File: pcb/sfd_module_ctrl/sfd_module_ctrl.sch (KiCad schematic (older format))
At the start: 12 parts

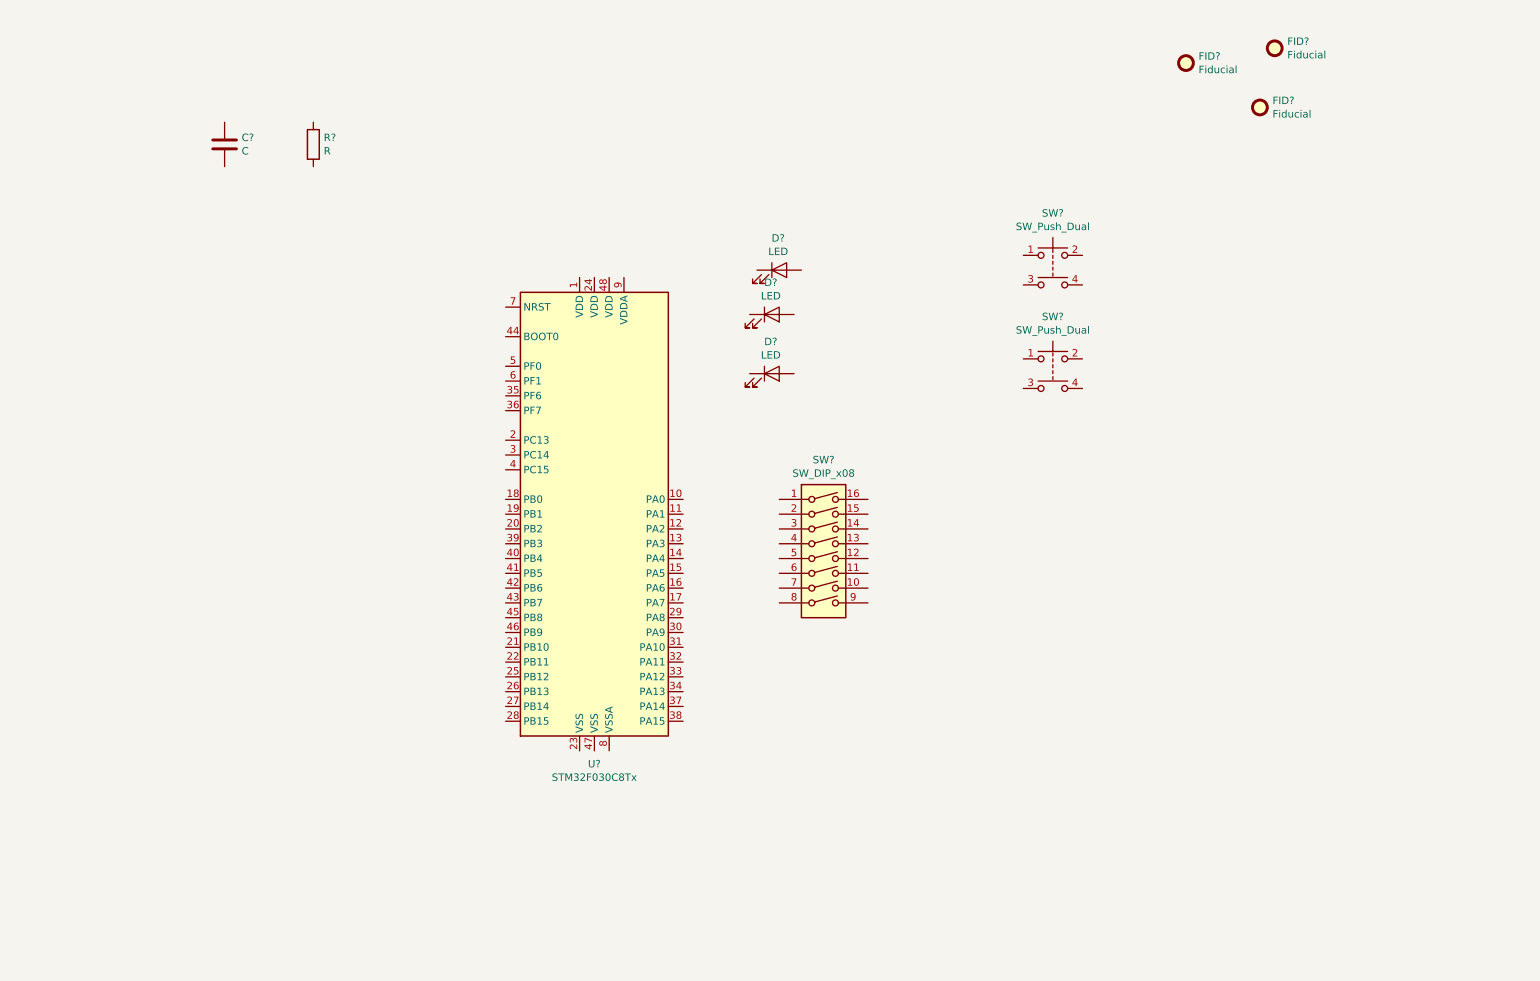
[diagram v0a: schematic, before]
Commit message: schematic progress, added stm32cubeMX generated chip config
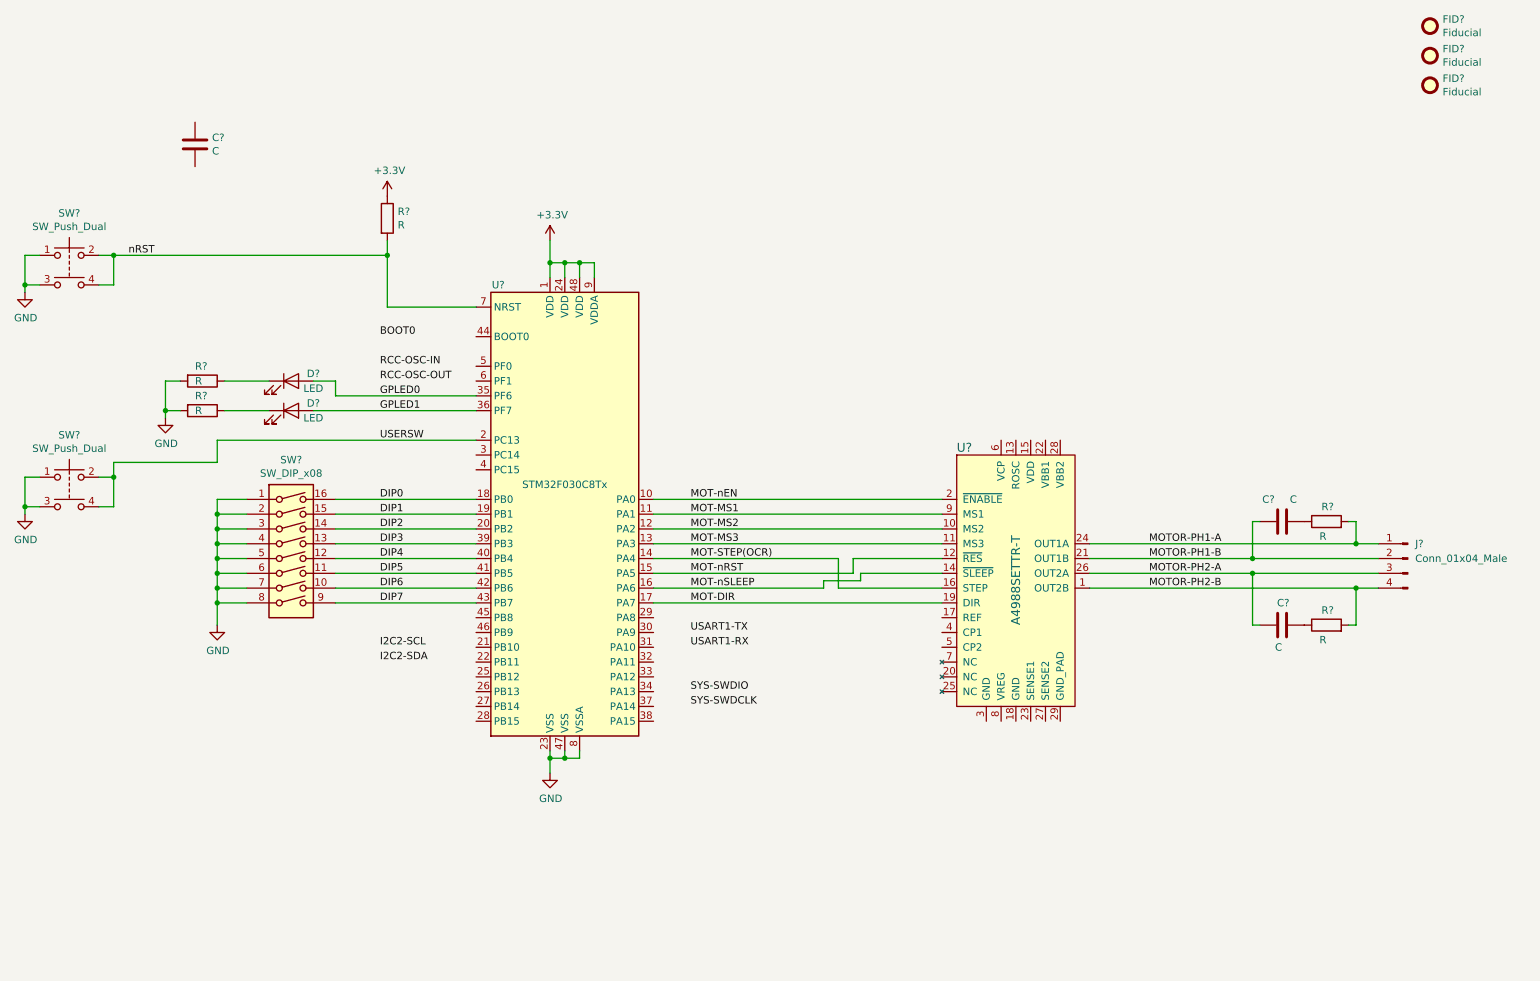
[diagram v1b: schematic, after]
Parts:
- removed D? (x2): LED, symbol Device:LED
- added C? (x2): C, symbol Device:C
- added D?: LED, symbol Device:LED
- added J?: Conn_01x04_Male, symbol Connector:Conn_01x04_Male
- added R? (x4): R, symbol Device:R
- added U?: A4988SETTR-T, digikey-footprints:VFQFN-28-1EP_5x5mm, symbol dk_PMIC-Motor-Drivers-Controllers:A4988SETTR-T
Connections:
- net +3V3: now reaches R?.1
- net +3V3: now also U?.1 (VDD), U?.24 (VDD), U?.48 (VDD), U?.9 (VDDA)
- net nRST: now reaches R?.2
- net nRST: now also SW?.2, SW?.4, U?.7 (NRST)
- net at D?.1 (K): now also R?.1
- net GPLED1: now reaches D?.2 (A)
- net GPLED1: now also U?.36 (PF7)
- net GND: now reaches SW?.1
- net GND: now also SW?.1, SW?.1, SW?.2, SW?.3, SW?.3, SW?.3, SW?.4, SW?.5, SW?.6, SW?.7, SW?.8, U?.23 (VSS), U?.47 (VSS), U?.8 (VSSA), R?.2, R?.2
- net DIP6: now reaches SW?.10
- net DIP6: now also U?.42 (PB6)
- net DIP5: now reaches SW?.11
- net DIP5: now also U?.41 (PB5)
- net DIP4: now reaches SW?.12
- net DIP4: now also U?.40 (PB4)
- net DIP3: now reaches SW?.13
- net DIP3: now also U?.39 (PB3)
- net DIP2: now reaches SW?.14
- net DIP2: now also U?.20 (PB2)
- net DIP1: now reaches SW?.15
- net DIP1: now also U?.19 (PB1)
- net DIP0: now reaches SW?.16
- net DIP0: now also U?.18 (PB0)
- net DIP7: now reaches SW?.9
- net DIP7: now also U?.43 (PB7)
- net MOT-nEN: now reaches U?.10 (PA0)
- net MOT-nEN: now also U?.2 (~ENABLE)
- net MOT-MS1: now reaches U?.11 (PA1)
- net MOT-MS1: now also U?.9 (MS1)
- net MOT-MS2: now reaches U?.12 (PA2)
- net MOT-MS2: now also U?.10 (MS2)
- net MOT-MS3: now reaches U?.13 (PA3)
- net MOT-MS3: now also U?.11 (MS3)
- net MOT-STEP(OCR): now reaches U?.14 (PA4)
- net MOT-STEP(OCR): now also U?.16 (STEP)
- net MOT-nRST: now reaches U?.15 (PA5)
- net MOT-nRST: now also U?.12 (~RES)
- net MOT-nSLEEP: now reaches U?.16 (PA6)
- net MOT-nSLEEP: now also U?.14 (~SLEEP)
- net MOT-DIR: now reaches U?.17 (PA7)
- net MOT-DIR: now also U?.19 (DIR)
- net USERSW: now reaches U?.2 (PC13)
- net USERSW: now also SW?.2, SW?.4
- net GPLED0: now reaches U?.35 (PF6)
- net GPLED0: now also D?.2 (A)
- new net: D?.1 (K), R?.1
- new net: C?.2, R?.1 (x2)
- new net MOTOR-PH1-A: J?.1 (Pin_1), R?.2, U?.24 (OUT1A)
- new net MOTOR-PH1-B: C?.1, J?.2 (Pin_2), U?.21 (OUT1B)
- new net MOTOR-PH2-A: C?.1, J?.3 (Pin_3), U?.26 (OUT2A)
- new net MOTOR-PH2-B: J?.4 (Pin_4), R?.2, U?.1 (OUT2B)
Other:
- moved on the sheet: C?, D?, FID?, R?, SW?, U?

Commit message: Added in-process photo, updated design_notes.md
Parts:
- added C? (x6): C, symbol Device:C
- added J?: Conn_02x06_Odd_Even, symbol Connector_Generic:Conn_02x06_Odd_Even
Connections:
- net +3V3: now also C?.2, C?.2, C?.2, C?.2
- net GND: now also C?.1, C?.1, C?.1, C?.1, C?.2, C?.2, J?.10 (Pin_10), J?.11 (Pin_11), J?.12 (Pin_12), J?.9 (Pin_9)
- net I2C2-SCL: now also J?.7 (Pin_7)
- net I2C2-SDA: now also J?.8 (Pin_8)
- net USERSW: now also C?.1
- net nRST: now also C?.1
- new net +12V: J?.1 (Pin_1), J?.2 (Pin_2), J?.3 (Pin_3), J?.4 (Pin_4)
